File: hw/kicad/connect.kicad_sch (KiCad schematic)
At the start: 28 parts

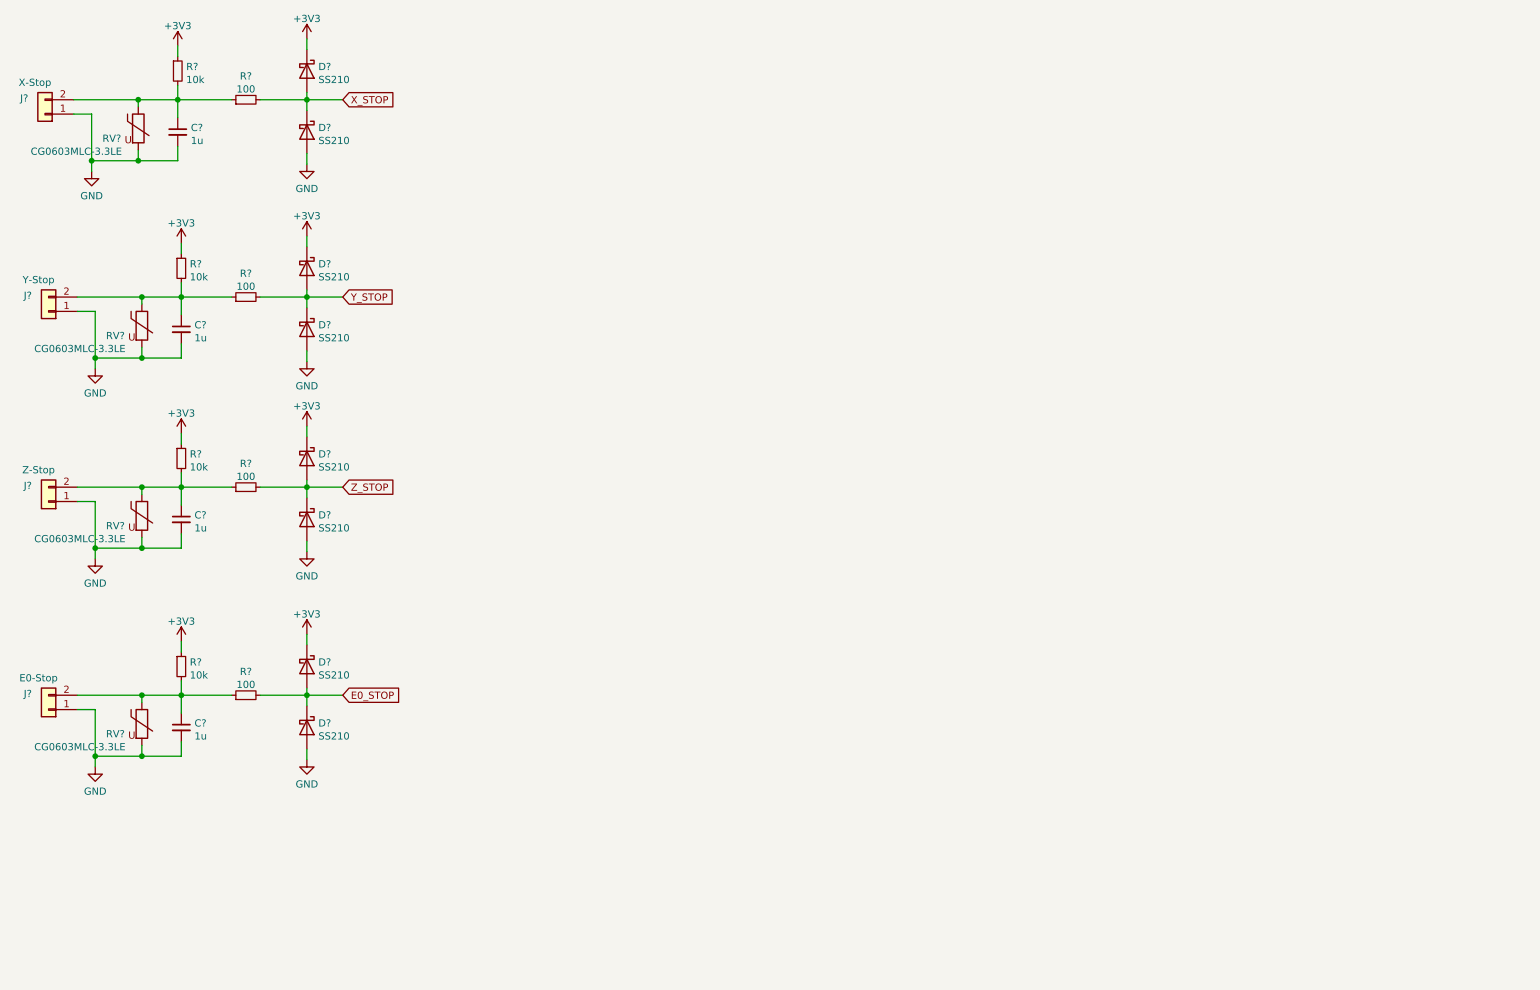
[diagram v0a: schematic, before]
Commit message: HW - schematics - added some connectors
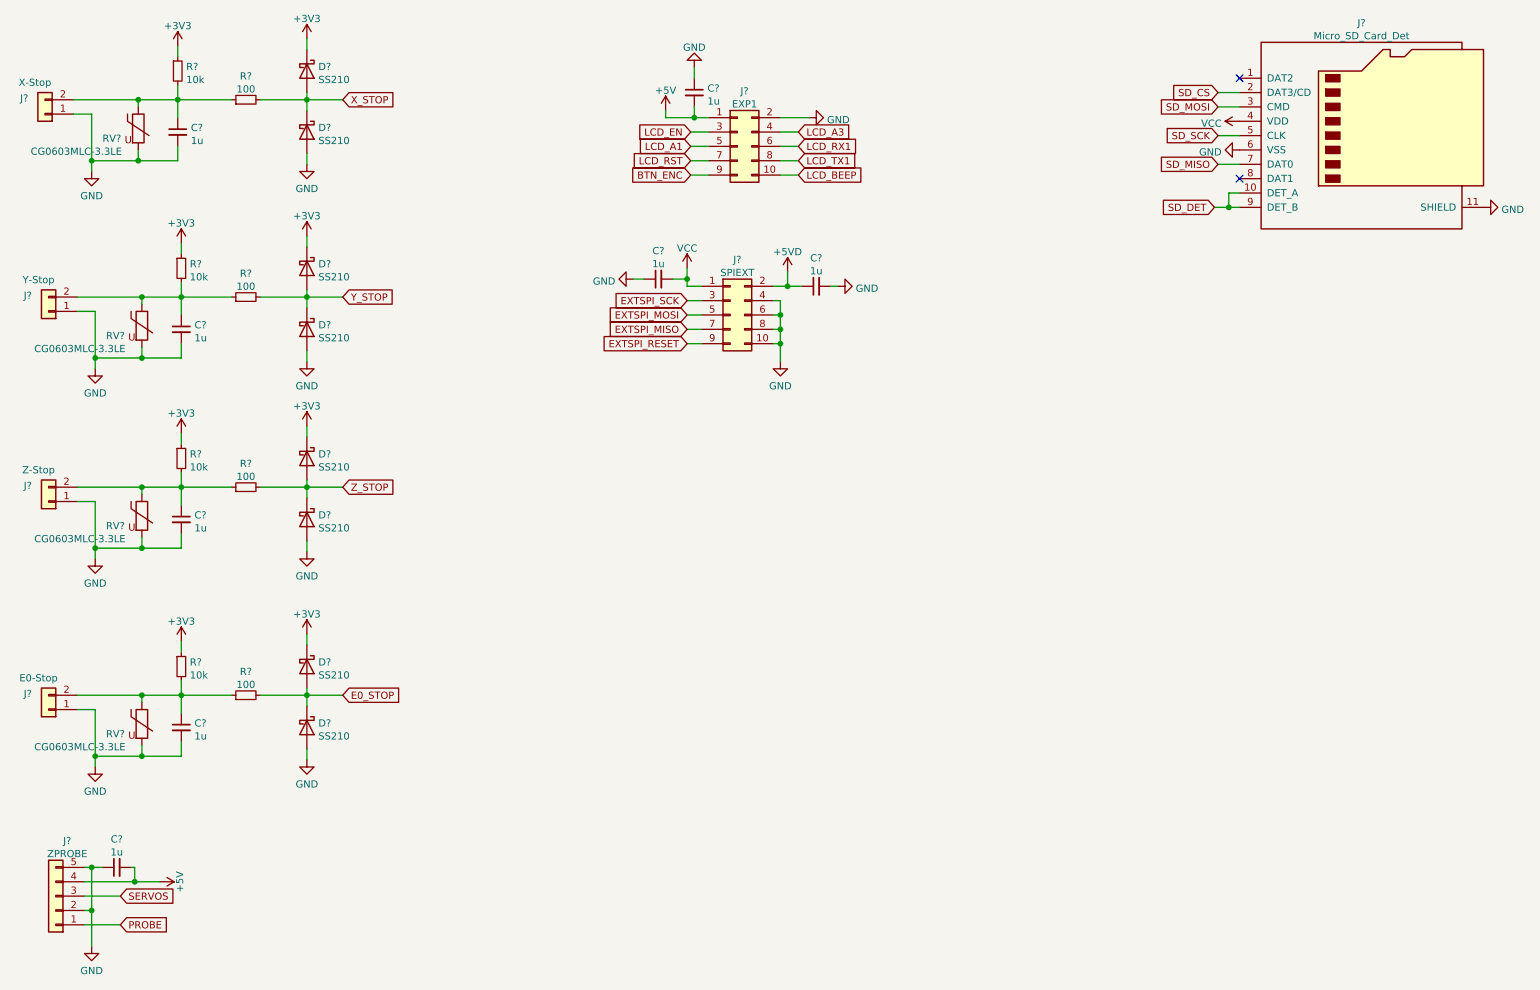
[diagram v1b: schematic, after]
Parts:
- added C? (x4): 1u, symbol Device:C_Small
- added J?: SPIEXT, symbol Connector_Generic:Conn_02x05_Odd_Even
- added J?: EXP1, symbol Connector_Generic:Conn_02x05_Odd_Even
- added J?: ZPROBE, symbol Connector_Generic:Conn_01x05
- added J?: Micro_SD_Card_Det, symbol Connector:Micro_SD_Card_Det
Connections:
- net GND: now also C?.1, C?.1, C?.1, C?.2, J?.10 (Pin_10), J?.11 (SHIELD), J?.2 (Pin_2), J?.2 (Pin_2), J?.4 (Pin_4), J?.5 (Pin_5), J?.6 (Pin_6), J?.6 (VSS), J?.8 (Pin_8)
- new net +5V: C?.2, C?.2, J?.1 (Pin_1), J?.4 (Pin_4)
- new net +5VD: C?.1, J?.2 (Pin_2)
- new net BTN_ENC: J?.9 (Pin_9)
- new net EXTSPI_MISO: J?.7 (Pin_7)
- new net EXTSPI_MOSI: J?.5 (Pin_5)
- new net EXTSPI_RESET: J?.9 (Pin_9)
- new net EXTSPI_SCK: J?.3 (Pin_3)
- new net LCD_A1: J?.5 (Pin_5)
- new net LCD_A3: J?.4 (Pin_4)
- new net LCD_BEEP: J?.10 (Pin_10)
- new net LCD_EN: J?.3 (Pin_3)
- new net LCD_RST: J?.7 (Pin_7)
- new net LCD_RX1: J?.6 (Pin_6)
- new net LCD_TX1: J?.8 (Pin_8)
- new net PROBE: J?.1 (Pin_1)
- new net SD_CS: J?.2 (DAT3/CD)
- new net SD_DET: J?.10 (DET_A), J?.9 (DET_B)
- new net SD_MISO: J?.7 (DAT0)
- new net SD_MOSI: J?.3 (CMD)
- new net SD_SCK: J?.5 (CLK)
- new net SERVOS: J?.3 (Pin_3)
- new net VCC: C?.2, J?.1 (Pin_1), J?.4 (VDD)
- no-connect marks 0 -> 2

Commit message: mcu
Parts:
- C73, C74, C75, C76, C77, C78, C79, C80: renamed from C?; footprint (none) -> Capacitor_SMD:C_0603_1608Metric
- R25, R26, R27, R28, R29, R30, R31, R32: renamed from R?; footprint (none) -> Resistor_SMD:R_0603_1608Metric
- gave numbers to parts that had none: 20

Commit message: hw schematics
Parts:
- added C?: 1u, Capacitor_SMD:C_0603_1608Metric, symbol Device:C_Small
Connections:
- net GND: now also C?.2
- net VCC: now also C?.1
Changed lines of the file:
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@@
   (junction (at 153.67 67.945) (diameter 1.016) (color 0 0 0 0))
   (junction (at 154.94 57.785) (diameter 1.016) (color 0 0 0 0))
+  (junction (at 210.185 28.575) (diameter 1.016) (color 0 0 0 0))
   (junction (at 233.045 43.815) (diameter 1.016) (color 0 0 0 0))
   (no_connect (at 234.95 20.955))
@@
     (stroke (width 0) (type solid) (color 0 0 0 0))
   )
+  (wire (pts (xy 208.28 28.575) (xy 210.185 28.575))
+    (stroke (width 0) (type solid) (color 0 0 0 0))
+  )
+  (wire (pts (xy 210.185 28.575) (xy 234.95 28.575))
+    (stroke (width 0) (type solid) (color 0 0 0 0))
+  )
+  (wire (pts (xy 210.185 29.845) (xy 210.185 28.575))
+    (stroke (width 0) (type solid) (color 0 0 0 0))
+  )
+  (wire (pts (xy 210.185 36.83) (xy 210.185 34.925))
+    (stroke (width 0) (type solid) (color 0 0 0 0))
+  )
   (wire (pts (xy 231.14 26.035) (xy 234.95 26.035))
     (stroke (width 0) (type solid) (color 0 0 0 0))
@@
     (pin "1")
   )
-  (symbol (lib_id "power:VCC") (at 234.95 28.575 90) (unit 1)
-    (in_bom yes) (on_board yes) (fields_autoplaced)
-    (property "Reference" "#PWR091" (id 0) (at 238.76 28.575 0)
-      (effects (font (size 1.27 1.27)) hide)
-    )
-    (property "Value" "VCC" (id 1) (at 231.7749 28.9635 90)
-      (effects (font (size 1.27 1.27)) (justify left))
-    )
-    (property "Footprint" "" (id 2) (at 234.95 28.575 0)
-      (effects (font (size 1.27 1.27)) hide)
-    )
-    (property "Datasheet" "" (id 3) (at 234.95 28.575 0)
+  (symbol (lib_id "power:VCC") (at 208.28 28.575 90) (unit 1)
+    (in_bom yes) (on_board yes) (fields_autoplaced)
+    (property "Reference" "#PWR091" (id 0) (at 212.09 28.575 0)
+      (effects (font (size 1.27 1.27)) hide)
+    )
+    (property "Value" "VCC" (id 1) (at 205.1049 28.9635 90)
+      (effects (font (size 1.27 1.27)) (justify left))
+    )
+    (property "Footprint" "" (id 2) (at 208.28 28.575 0)
+      (effects (font (size 1.27 1.27)) hide)
+    )
+    (property "Datasheet" "" (id 3) (at 208.28 28.575 0)
       (effects (font (size 1.27 1.27)) hide)
     )
@@
     )
     (property "Datasheet" "" (id 3) (at 163.83 57.785 0)
+      (effects (font (size 1.27 1.27)) hide)
+    )
+    (pin "1")
+  )
+  (symbol (lib_id "power:GND") (at 210.185 36.83 0) (unit 1)
+    (in_bom yes) (on_board yes) (fields_autoplaced)
+    (property "Reference" "#PWR?" (id 0) (at 210.185 43.18 0)
+      (effects (font (size 1.27 1.27)) hide)
+    )
+    (property "Value" "GND" (id 1) (at 210.185 41.1544 0))
+    (property "Footprint" "" (id 2) (at 210.185 36.83 0)
+      (effects (font (size 1.27 1.27)) hide)
+    )
+    (property "Datasheet" "" (id 3) (at 210.185 36.83 0)
       (effects (font (size 1.27 1.27)) hide)
     )
@@
       (effects (font (size 1.27 1.27)) hide)
     )
+    (pin "1")
+    (pin "2")
+  )
+  (symbol (lib_id "Device:C_Small") (at 210.185 32.385 0) (unit 1)
+    (in_bom yes) (on_board yes) (fields_autoplaced)
+    (property "Reference" "C?" (id 0) (at 212.5092 31.6241 0)
+      (effects (font (size 1.27 1.27)) (justify left))
+    )
+    (property "Value" "1u" (id 1) (at 212.5092 33.9228 0)
+      (effects (font (size 1.27 1.27)) (justify left))
+    )
+    (property "Footprint" "Capacitor_SMD:C_0603_1608Metric" (id 2) (at 210.185 32.385 0)
+      (effects (font (size 1.27 1.27)) hide)
+    )
+    (property "Datasheet" "~" (id 3) (at 210.185 32.385 0)
+      (effects (font (size 1.27 1.27)) hide)
+    )
